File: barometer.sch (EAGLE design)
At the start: 88 parts, among them IC1 MIC5225-3.3v, IC2 TPS5410, IC3 ZPA2326-0311A-R, U1 MCP4725, U2 LTC2850, U3 PCA9306, U4 MAX3221, U5 XC6215XC6215B182NR, U6 Tiny85-20-SMT, X2 1751264, X3 1751248

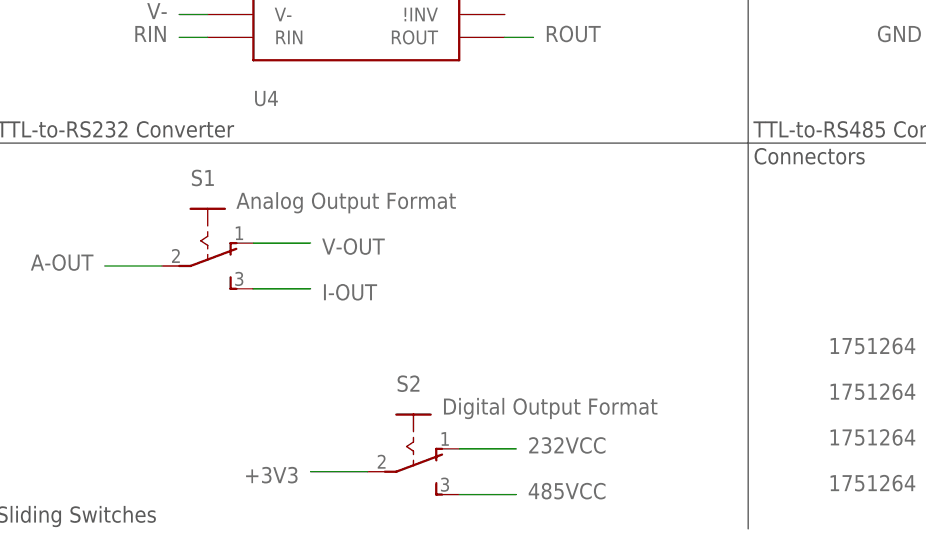
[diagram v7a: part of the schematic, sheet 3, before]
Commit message: Substitute through-hole SPDT sliding switch
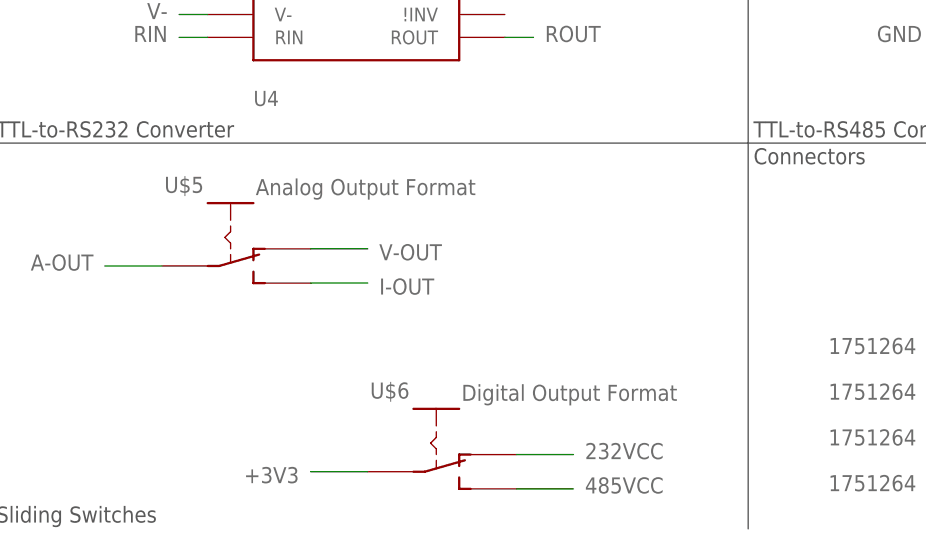
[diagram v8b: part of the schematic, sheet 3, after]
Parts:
- removed S1: Analog Output Format, switch:255SB
- removed S2: Digital Output Format, switch:255SB
- added U$5: Analog Output Format, switch-daier:SS12F21
- added U$6: Digital Output Format, switch-daier:SS12F21
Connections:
- net +3V3: now also U$6.COMMON; no longer S2.P
- net 232VCC: now also U$6.SLIDE-1; no longer S2.O
- net 485VCC: now also U$6.SLIDE-2; no longer S2.S
- net A-OUT: now also U$5.COMMON; no longer S1.P
- net I-OUT: now also U$5.SLIDE-2; no longer S1.S
- net V-OUT: now also U$5.SLIDE-1; no longer S1.O
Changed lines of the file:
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@@
 <part name="X3" library="con-phoenix-350" deviceset="1751248" device=""/>
 <part name="X2" library="con-phoenix-350" deviceset="1751264" device=""/>
-<part name="S1" library="switch" deviceset="255SB" device="" value="Analog Output Format"/>
-<part name="S2" library="switch" deviceset="255SB" device="" value="Digital Output Format"/>
 <part name="U3" library="SparkFun-IC-Comms" deviceset="PCA9306" device="" value="PCA9306"/>
 <part name="SJ10" library="SparkFun-Retired" deviceset="SOLDERJUMPER" device="TRACE"/>
@@
 <part name="TP15" library="testpad" deviceset="PTR1" device="B1,27"/>
 <part name="TP16" library="testpad" deviceset="PTR1" device="B1,27"/>
+<part name="U$5" library="switch-daier" deviceset="SS" device="12F21" value="Analog Output Format"/>
+<part name="U$6" library="switch-daier" deviceset="SS" device="12F21" value="Digital Output Format"/>
 </parts>
 <sheets>
@@
 <instance part="X2" gate="-3" x="120.65" y="13.97" rot="R180"/>
 <instance part="X2" gate="-4" x="120.65" y="8.89" rot="R180"/>
-<instance part="S1" gate="1" x="27.94" y="35.56" rot="R270"/>
-<instance part="S2" gate="1" x="50.8" y="12.7" rot="R270"/>
 <instance part="TP15" gate="G$1" x="58.42" y="153.67"/>
 <instance part="TP16" gate="G$1" x="63.5" y="153.67"/>
+<instance part="U$5" gate="G$1" x="30.48" y="33.02" smashed="yes">
+<attribute name="NAME" x="23.114" y="41.148" size="1.778" layer="95"/>
+<attribute name="VALUE" x="33.274" y="40.894" size="1.778" layer="95"/>
+</instance>
+<instance part="U$6" gate="G$1" x="53.34" y="10.16" smashed="yes">
+<attribute name="NAME" x="45.974" y="18.288" size="1.778" layer="95"/>
+<attribute name="VALUE" x="56.134" y="18.034" size="1.778" layer="95"/>
+</instance>
 </instances>
 <busses>
@@
 <wire x1="39.37" y1="10.16" x2="45.72" y2="10.16" width="0.1524" layer="91"/>
 <label x="38.1" y="8.89" size="1.778" layer="95" font="vector" rot="MR0"/>
-<pinref part="S2" gate="1" pin="P"/>
+<pinref part="U$6" gate="G$1" pin="COMMON"/>
 </segment>
 <segment>
@@
 </segment>
 <segment>
-<wire x1="55.88" y1="12.7" x2="62.23" y2="12.7" width="0.1524" layer="91"/>
-<label x="63.5" y="13.97" size="1.778" layer="95" font="vector" rot="MR180"/>
-<pinref part="S2" gate="1" pin="O"/>
+<wire x1="62.23" y1="12.065" x2="68.58" y2="12.065" width="0.1524" layer="91"/>
+<label x="69.85" y="13.335" size="1.778" layer="95" font="vector" rot="MR180"/>
+<pinref part="U$6" gate="G$1" pin="SLIDE-1"/>
 </segment>
 </net>
@@
 </segment>
 <segment>
-<wire x1="55.88" y1="7.62" x2="62.23" y2="7.62" width="0.1524" layer="91"/>
-<label x="63.5" y="8.89" size="1.778" layer="95" font="vector" rot="MR180"/>
-<pinref part="S2" gate="1" pin="S"/>
+<wire x1="62.23" y1="8.255" x2="68.58" y2="8.255" width="0.1524" layer="91"/>
+<label x="69.85" y="9.525" size="1.778" layer="95" font="vector" rot="MR180"/>
+<pinref part="U$6" gate="G$1" pin="SLIDE-2"/>
 </segment>
 </net>
@@
 <wire x1="22.86" y1="33.02" x2="16.51" y2="33.02" width="0.1524" layer="91"/>
 <label x="15.24" y="34.29" size="1.778" layer="95" font="vector" rot="R180"/>
-<pinref part="S1" gate="1" pin="P"/>
+<pinref part="U$5" gate="G$1" pin="COMMON"/>
 </segment>
 </net>
@@
 </segment>
 <segment>
-<wire x1="39.37" y1="35.56" x2="33.02" y2="35.56" width="0.1524" layer="91"/>
-<label x="40.64" y="34.29" size="1.778" layer="95" font="vector"/>
-<pinref part="S1" gate="1" pin="O"/>
+<wire x1="45.72" y1="34.925" x2="39.37" y2="34.925" width="0.1524" layer="91"/>
+<label x="46.99" y="33.655" size="1.778" layer="95" font="vector"/>
+<pinref part="U$5" gate="G$1" pin="SLIDE-1"/>
 </segment>
 <segment>
@@
 <net name="I-OUT" class="0">
 <segment>
-<wire x1="39.37" y1="30.48" x2="33.02" y2="30.48" width="0.1524" layer="91"/>
-<label x="40.64" y="29.21" size="1.778" layer="95" font="vector"/>
-<pinref part="S1" gate="1" pin="S"/>
-</segment>
-<segment>
+<wire x1="45.72" y1="31.115" x2="39.37" y2="31.115" width="0.1524" layer="91"/>
+<label x="46.99" y="29.845" size="1.778" layer="95" font="vector"/>
+<pinref part="U$5" gate="G$1" pin="SLIDE-2"/>
+</segment>
+<segment>
